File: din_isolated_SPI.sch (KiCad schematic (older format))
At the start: 20 parts, among them J1 CONN_01X10, U1 SI8661AB-B-IS1, U4 WeMos_mini

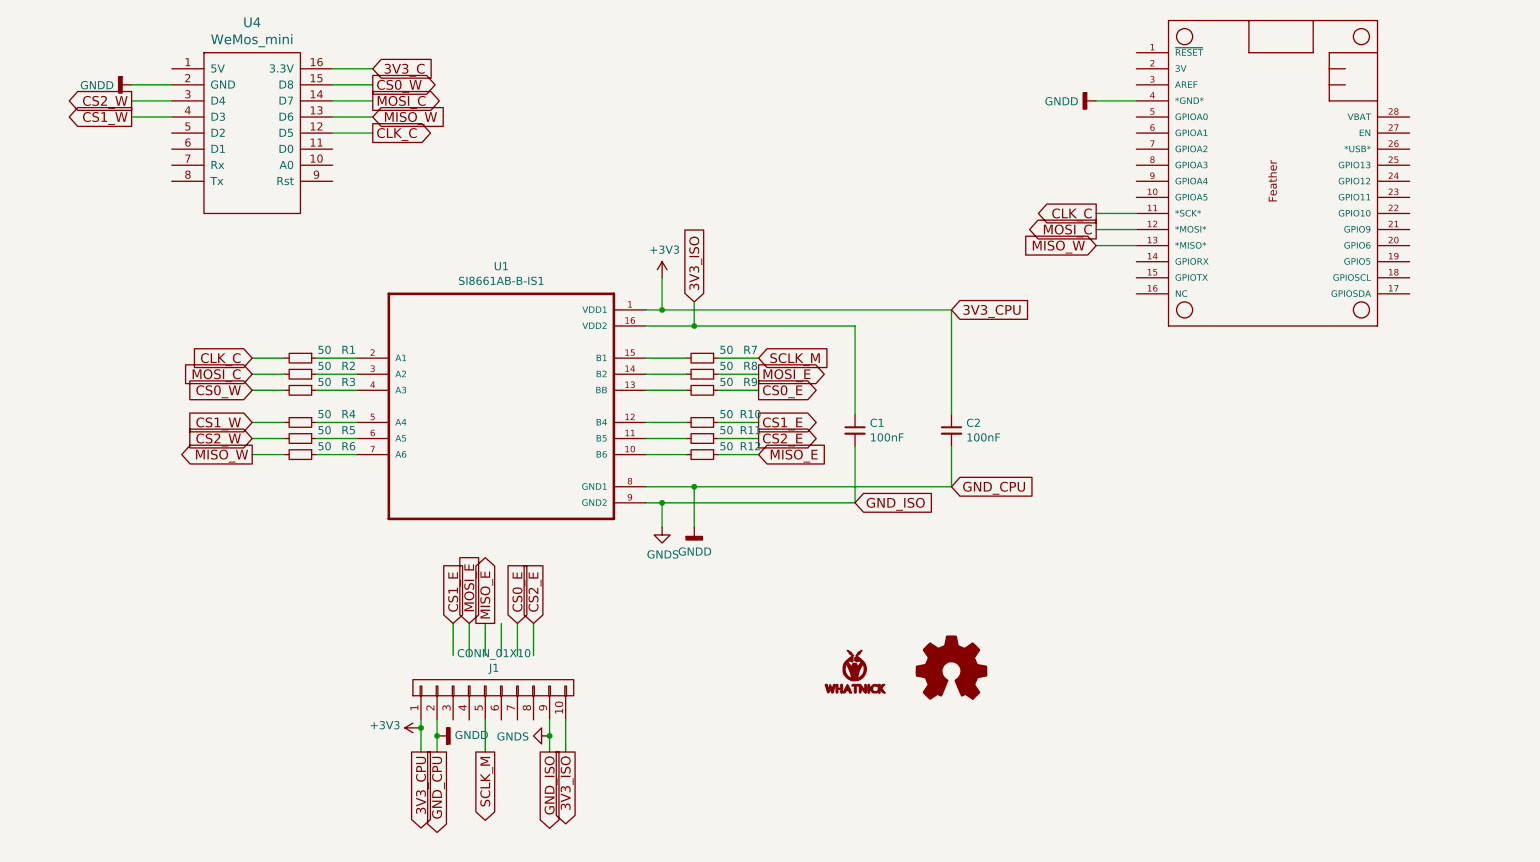
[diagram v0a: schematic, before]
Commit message: First pass at evolution of Tisham's board.
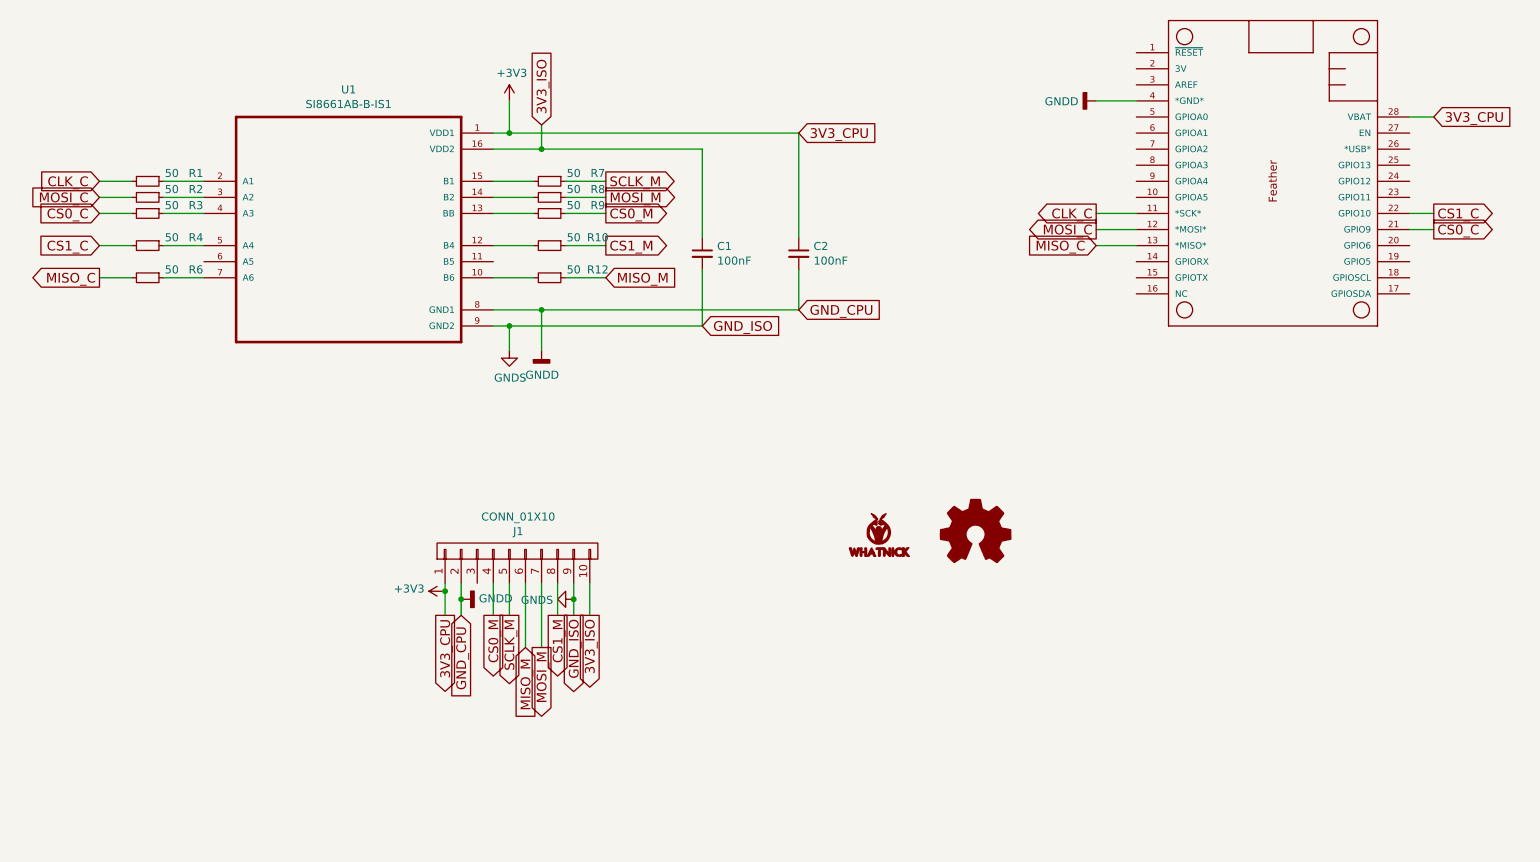
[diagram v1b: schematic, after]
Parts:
- removed R11, R5: 50, Resistors_SMD:R_0603, symbol device:R_Small
- removed U4: WeMos_mini, wemos_d1_mini:D1_mini_board, symbol wemos_mini:WeMos_mini
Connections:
- net labels added: CS0_C, CS0_M, CS1_C, CS1_M, MISO_C, MISO_M, MOSI_M
- net labels removed: 3V3_C, CS0_E, CS0_W, CS1_E, CS1_W, CS2_E, CS2_W, MISO_E, MISO_W, MOSI_E
- wire segments 66 -> 55
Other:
- moved on the sheet: C1, C2, J1, R1, R10, R12, R2, R3, R4, R6, R7, R8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

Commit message: PCB submitted to OSH Park.  BoM created.
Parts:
- removed LOGO1: Logo_Open_Hardware_Small, Symbols:OSHW-Symbol_6.7x6mm_SilkScreen, symbol din_isolated_SPI-rescue:Logo_Open_Hardware_Small-RESCUE-din_isolated_SPI
- C1, C2: value 100nF -> .1u; footprint Capacitors_SMD:C_0603 -> Capacitor_SMD:C_0805_2012Metric; PN (none) -> C
- G1: PN (none) -> X
- J1: PN (none) -> 53290-1080
- MS1: renamed from MS?; footprint (none) -> HappyDayEnergyMonitor:ADAFRUIT_FEATHER; PN (none) -> X
- R1, R10, R12, R2, R3, R4, R6, R7, R8, R9: value 50 -> 47; footprint Resistors_SMD:R_0603 -> Resistor_SMD:R_0805_2012Metric; PN (none) -> R
- U1: PN (none) -> SI8661AB-B-IS1
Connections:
- net 3V3_ISO renamed 3V3_M
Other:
- moved on the sheet: J1
